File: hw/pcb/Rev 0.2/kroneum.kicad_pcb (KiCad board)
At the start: 2 copper layers, 50 x 40 mm, 18 parts, among them J1 USB_B_Micro, J2 SWD_I2C_BOOT, SW1 Boot_Mode_Btn, SW2 Ctrl_One_Btn, SW3 Reset_Btn, SW4 Ctrl_Ten_Btn, U1 STM32F042F4Px

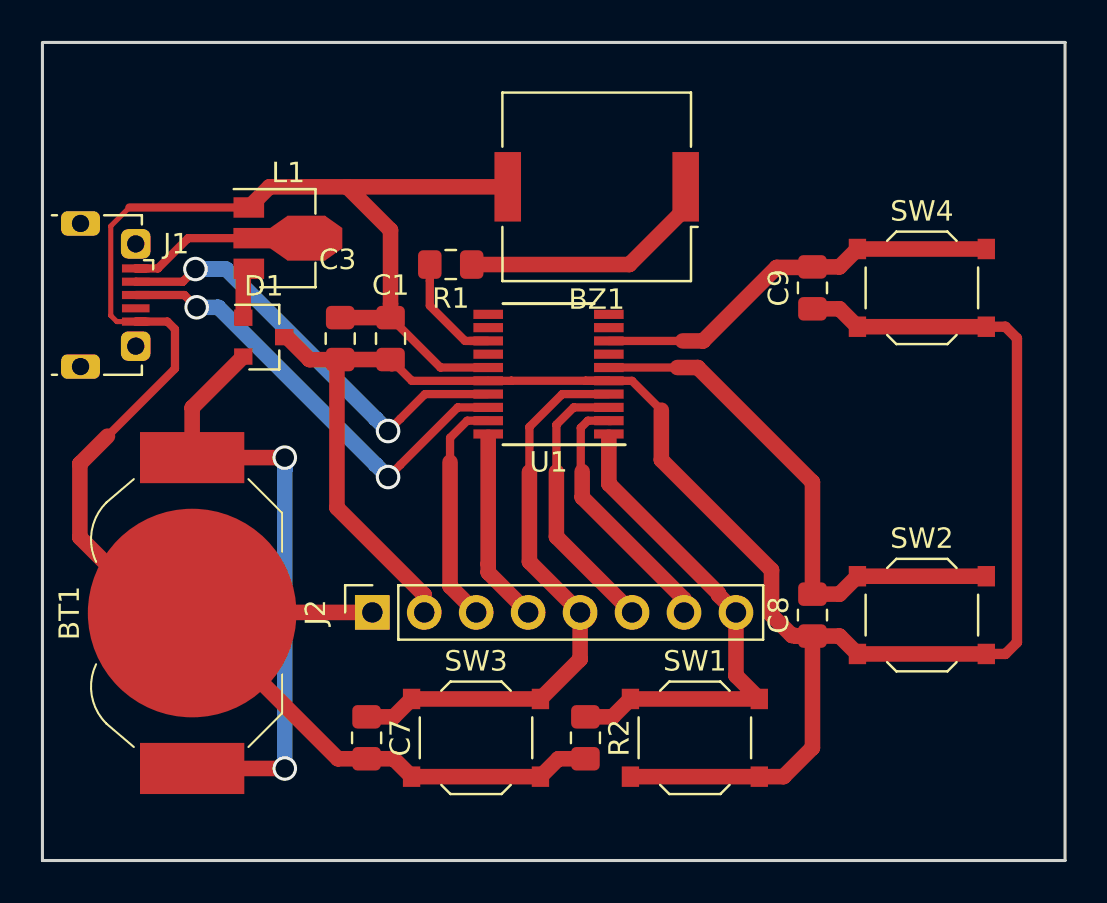
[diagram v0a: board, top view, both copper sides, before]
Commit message: hw: pcb remove redundant traces.
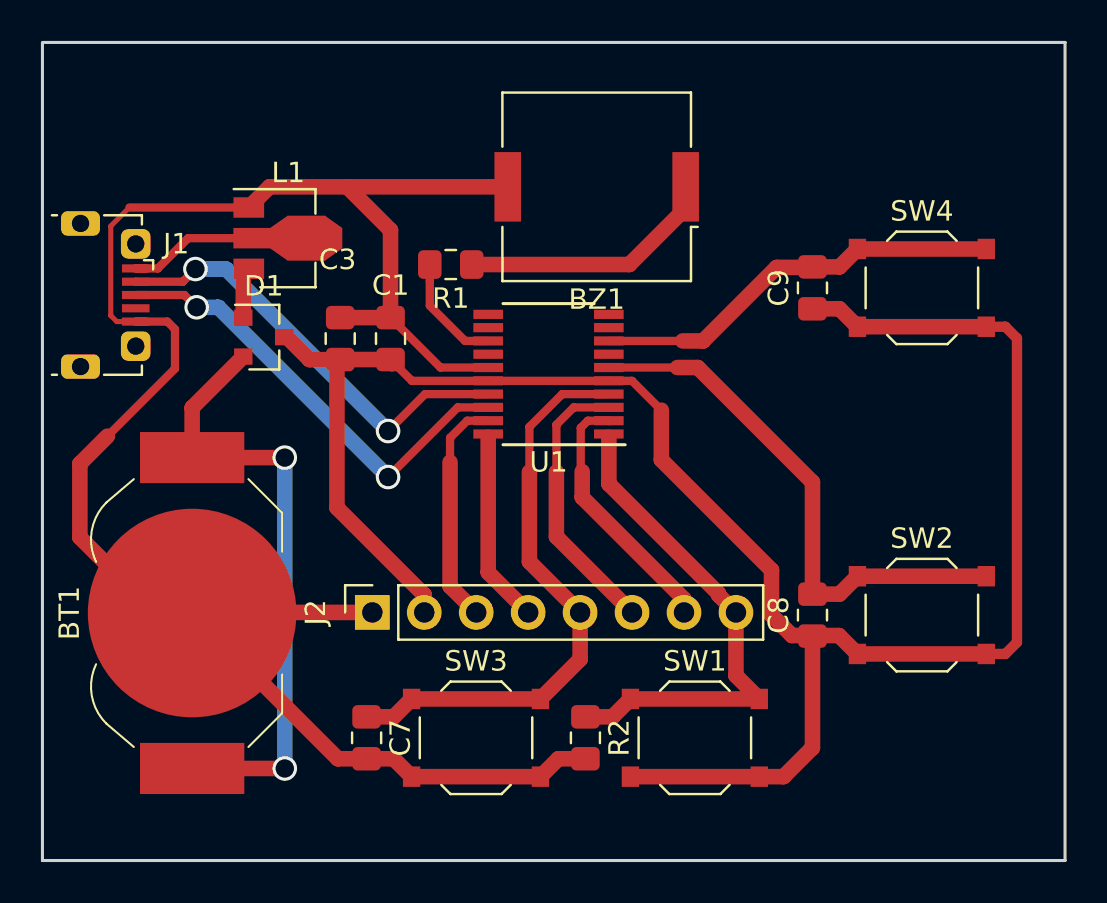
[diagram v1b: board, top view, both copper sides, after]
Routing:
- net SWCLK: track 15.7 -> 9.38 mm
- net GND: track 101.8 -> 97.9 mm
- net VDD: track 101.0 -> 99.9 mm
- net Buzzer: track 6.49 -> 5.58 mm
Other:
- rule trace_min: 0.2 -> 0.25
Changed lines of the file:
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@@
     (thickness 1.6)
     (drawings 4)
-    (tracks 186)
+    (tracks 167)
     (zones 0)
     (modules 18)
@@
   )
   (setup
-    (last_trace_width 0.762)
+    (last_trace_width 0.4064)
     (user_trace_width 0.4064)
     (user_trace_width 0.4572)
@@
     (zone_clearance 0.508)
     (zone_45_only no)
-    (trace_min 0.2)
+    (trace_min 0.25)
     (segment_width 0.2)
     (edge_width 0.15)
@@
   (segment (start 127.83 107.02) (end 127.83 108.951011) (width 0.4064) (layer F.Cu) (net 1))
   (segment (start 125.9125 106.65) (end 127.46 106.65) (width 0.4064) (layer F.Cu) (net 1))
-  (segment (start 123.180001 117.200001) (end 125.88 119.9) (width 0.4064) (layer F.Cu) (net 1))
   (segment (start 125.6 101.07) (end 131.44 101.07) (width 0.4064) (layer F.Cu) (net 1))
   (segment (start 140.81 108.895) (end 138.37 106.455) (width 0.4064) (layer F.Cu) (net 1))
   (segment (start 143.145 108.895) (end 140.81 108.895) (width 0.4064) (layer F.Cu) (net 1))
-  (segment (start 138.37 105.78) (end 138.37 106.455) (width 0.762) (layer F.Cu) (net 1))
   (segment (start 131.44 101.07) (end 131.69 101.07) (width 0.762) (layer F.Cu) (net 1))
   (segment (start 147.864729 127.955) (end 148.2 127.955) (width 0.4064) (layer F.Cu) (net 1))
@@
   (segment (start 135.91 106.455) (end 138.37 106.455) (width 0.762) (layer F.Cu) (net 1))
   (segment (start 132.45 100.06) (end 131.44 101.07) (width 0.762) (layer F.Cu) (net 1))
-  (segment (start 138.37 102.18) (end 138.37 105.78) (width 0.762) (layer F.Cu) (net 1))
-  (segment (start 136.25 100.06) (end 138.37 102.18) (width 0.762) (layer F.Cu) (net 1))
   (segment (start 144.1 100.06) (end 136.25 100.06) (width 0.762) (layer F.Cu) (net 1))
   (segment (start 136.25 100.06) (end 132.45 100.06) (width 0.762) (layer F.Cu) (net 1))
+  (segment (start 138.37 102.18) (end 138.37 106.455) (width 0.762) (layer F.Cu) (net 1))
+  (segment (start 136.25 100.06) (end 138.37 102.18) (width 0.762) (layer F.Cu) (net 1))
   (segment (start 152.8 101.11) (end 152.8 100.06) (width 0.762) (layer F.Cu) (net 2))
   (segment (start 150.05 103.86) (end 152.8 101.11) (width 0.762) (layer F.Cu) (net 2))
   (segment (start 142.34 103.86) (end 150.05 103.86) (width 0.762) (layer F.Cu) (net 2))
-  (segment (start 144.279903 109.541497) (end 144.2764 109.545) (width 0.4064) (layer F.Cu) (net 3))
-  (segment (start 144.2764 109.545) (end 143.145 109.545) (width 0.4064) (layer F.Cu) (net 3))
-  (segment (start 147.9136 109.545) (end 147.910097 109.541497) (width 0.4064) (layer F.Cu) (net 3))
-  (segment (start 149.045 109.545) (end 147.9136 109.545) (width 0.4064) (layer F.Cu) (net 3))
-  (segment (start 147.910097 109.541497) (end 144.279903 109.541497) (width 0.4064) (layer F.Cu) (net 3))
   (segment (start 138.435 108.9) (end 138.41 108.875) (width 0.4064) (layer F.Cu) (net 3))
-  (segment (start 149.045 109.545) (end 148.019238 109.545) (width 0.4064) (layer F.Cu) (net 3))
   (segment (start 139.41 109.545) (end 138.37 108.505) (width 0.4064) (layer F.Cu) (net 3))
   (segment (start 143.145 109.545) (end 139.41 109.545) (width 0.4064) (layer F.Cu) (net 3))
@@
   (segment (start 150.1764 109.545) (end 151.610789 110.979389) (width 0.4064) (layer F.Cu) (net 3))
   (segment (start 149.045 109.545) (end 150.1764 109.545) (width 0.4064) (layer F.Cu) (net 3))
-  (segment (start 160.325 122.025) (end 161.2 122.9) (width 0.762) (layer F.Cu) (net 3))
-  (segment (start 159 122.025) (end 160.325 122.025) (width 0.762) (layer F.Cu) (net 3))
   (segment (start 161.2 122.9) (end 167.5 122.9) (width 0.762) (layer F.Cu) (net 3))
   (segment (start 140.02 120.02) (end 140.02 120.87) (width 0.762) (layer F.Cu) (net 3))
@@
   (segment (start 156.4 128.9) (end 150.1 128.9) (width 0.762) (layer F.Cu) (net 3))
   (segment (start 151.610789 113.410789) (end 151.610789 110.979389) (width 0.762) (layer F.Cu) (net 3))
-  (segment (start 158.2 122.025) (end 158.175 122) (width 0.762) (layer F.Cu) (net 3))
   (segment (start 157 121) (end 157 118.8) (width 0.762) (layer F.Cu) (net 3))
-  (segment (start 159 122.025) (end 158.2 122.025) (width 0.762) (layer F.Cu) (net 3))
   (segment (start 158 122) (end 157 121) (width 0.762) (layer F.Cu) (net 3))
   (segment (start 157 118.8) (end 151.610789 113.410789) (width 0.762) (layer F.Cu) (net 3))
-  (segment (start 158.175 122) (end 158 122) (width 0.762) (layer F.Cu) (net 3))
+  (segment (start 143.145 109.545) (end 149.045 109.545) (width 0.4064) (layer F.Cu) (net 3))
+  (segment (start 160.3 122) (end 161.2 122.9) (width 0.762) (layer F.Cu) (net 3))
+  (segment (start 158 122) (end 160.3 122) (width 0.762) (layer F.Cu) (net 3))
   (segment (start 159 119.975) (end 159.275 119.975) (width 0.4064) (layer F.Cu) (net 4))
   (segment (start 149.045 108.895) (end 152.395 108.895) (width 0.4064) (layer F.Cu) (net 4))
@@
   (segment (start 128.230001 104.679999) (end 128.83 104.08) (width 0.4064) (layer F.Cu) (net 6))
   (segment (start 128.21 104.7) (end 128.230001 104.679999) (width 0.4064) (layer F.Cu) (net 6))
+  (via (at 138.25 112) (size 1.2) (drill 0.9) (layers F.Cu B.Cu) (net 6))
+  (segment (start 130.33 104.08) (end 138.25 112) (width 0.762) (layer B.Cu) (net 6))
+  (segment (start 128.83 104.08) (end 130.33 104.08) (width 0.762) (layer B.Cu) (net 6))
+  (segment (start 140.055 110.195) (end 138.25 112) (width 0.4064) (layer F.Cu) (net 6))
   (segment (start 143.145 110.195) (end 140.055 110.195) (width 0.4064) (layer F.Cu) (net 6))
-  (segment (start 128.83 104.08) (end 130.33 104.08) (width 0.762) (layer B.Cu) (net 6))
-  (via (at 138.25 112) (size 1.2) (drill 0.9) (layers F.Cu B.Cu) (net 6))
-  (segment (start 130.33 104.08) (end 137.650001 111.400001) (width 0.762) (layer B.Cu) (net 6))
-  (segment (start 140.055 110.195) (end 138.849999 111.400001) (width 0.4064) (layer F.Cu) (net 6))
-  (segment (start 137.650001 111.400001) (end 138.25 112) (width 0.762) (layer B.Cu) (net 6))
-  (segment (start 138.849999 111.400001) (end 138.25 112) (width 0.4064) (layer F.Cu) (net 6))
   (via (at 128.89 105.95) (size 1.2) (drill 0.9) (layers F.Cu B.Cu) (net 8))
   (segment (start 128.290001 105.350001) (end 128.89 105.95) (width 0.4064) (layer F.Cu) (net 8))
   (segment (start 125.9125 105.35) (end 128.290001 105.350001) (width 0.4064) (layer F.Cu) (net 8))
   (via (at 138.25 114.250008) (size 1.2) (drill 0.9) (layers F.Cu B.Cu) (net 8))
-  (segment (start 129.949992 105.95) (end 137.650001 113.650009) (width 0.762) (layer B.Cu) (net 8))
-  (segment (start 137.650001 113.650009) (end 138.25 114.250008) (width 0.762) (layer B.Cu) (net 8))
+  (segment (start 141.655008 110.845) (end 138.25 114.250008) (width 0.4064) (layer F.Cu) (net 8))
+  (segment (start 143.145 110.845) (end 141.655008 110.845) (width 0.4064) (layer F.Cu) (net 8))
+  (segment (start 129.949992 105.95) (end 138.25 114.250008) (width 0.762) (layer B.Cu) (net 8))
   (segment (start 128.89 105.95) (end 129.949992 105.95) (width 0.762) (layer B.Cu) (net 8))
-  (segment (start 138.849999 113.650009) (end 138.25 114.250008) (width 0.4064) (layer F.Cu) (net 8))
-  (segment (start 141.655008 110.845) (end 138.849999 113.650009) (width 0.4064) (layer F.Cu) (net 8))
-  (segment (start 143.145 110.845) (end 141.655008 110.845) (width 0.4064) (layer F.Cu) (net 8))
-  (segment (start 143.145 107.595) (end 142.233604 107.595) (width 0.4064) (layer F.Cu) (net 9))
   (segment (start 140.29 104.66) (end 140.29 103.86) (width 0.4064) (layer F.Cu) (net 9))
   (segment (start 140.29 105.8714) (end 140.29 104.66) (width 0.4064) (layer F.Cu) (net 9))
@@
   (segment (start 133.2 128.5) (end 133.2 128.5) (width 0.762) (layer F.Cu) (net 15))
   (via (at 133.2 128.5) (size 1.2) (drill 0.9) (layers F.Cu B.Cu) (net 15))
-  (segment (start 133.2 113.865685) (end 133.2 128.5) (width 0.762) (layer B.Cu) (net 15))
-  (segment (start 133.2 113.3) (end 133.2 113.865685) (width 0.762) (layer B.Cu) (net 15))
+  (segment (start 133.2 113.3) (end 133.2 128.5) (width 0.762) (layer B.Cu) (net 15))
   (segment (start 125.9125 104.05) (end 126.3875 104.05) (width 0.4064) (layer F.Cu) (net 16))
   (segment (start 125.9125 104.05) (end 126.409786 104.05) (width 0.25) (layer F.Cu) (net 16))
@@
   (segment (start 141.28 112.334238) (end 141.28 113.52) (width 0.4064) (layer F.Cu) (net 20))
   (segment (start 141.28 113.52) (end 141.28 119.59) (width 0.762) (layer F.Cu) (net 20))
-  (segment (start 143.145 118.915) (end 143.145 118.5) (width 0.762) (layer F.Cu) (net 21))
   (segment (start 145.1 120.87) (end 143.145 118.915) (width 0.762) (layer F.Cu) (net 21))
-  (segment (start 143.145 112.145) (end 143.145 118.5) (width 0.4064) (layer F.Cu) (net 21))
-  (segment (start 143.145 118.5) (end 143.145 112.301001) (width 0.762) (layer F.Cu) (net 21))
+  (segment (start 143.145 118.915) (end 143.145 112.301001) (width 0.762) (layer F.Cu) (net 21))
   (segment (start 149.045 111.495) (end 149.144999 111.594999) (width 0.25) (layer F.Cu) (net 22))
   (segment (start 149.045 111.495) (end 149.045 111.516799) (width 0.4064) (layer F.Cu) (net 22))
@@
   (segment (start 146.48 114) (end 146.48 117.17) (width 0.762) (layer F.Cu) (net 23))
   (segment (start 146.48 111.69) (end 146.48 114) (width 0.4064) (layer F.Cu) (net 23))
-  (segment (start 131.17 104.34) (end 131.44 104.07) (width 0.762) (layer F.Cu) (net 24))
   (segment (start 131.17 106.46) (end 131.17 104.34) (width 0.762) (layer F.Cu) (net 24))
 )
